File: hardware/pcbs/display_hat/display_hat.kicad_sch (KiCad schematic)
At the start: 13 parts, among them J1 WAVESHARE_HAT_HEADER, J2 MTA100_08, J3 MTA100_08, J4 MTA100_02

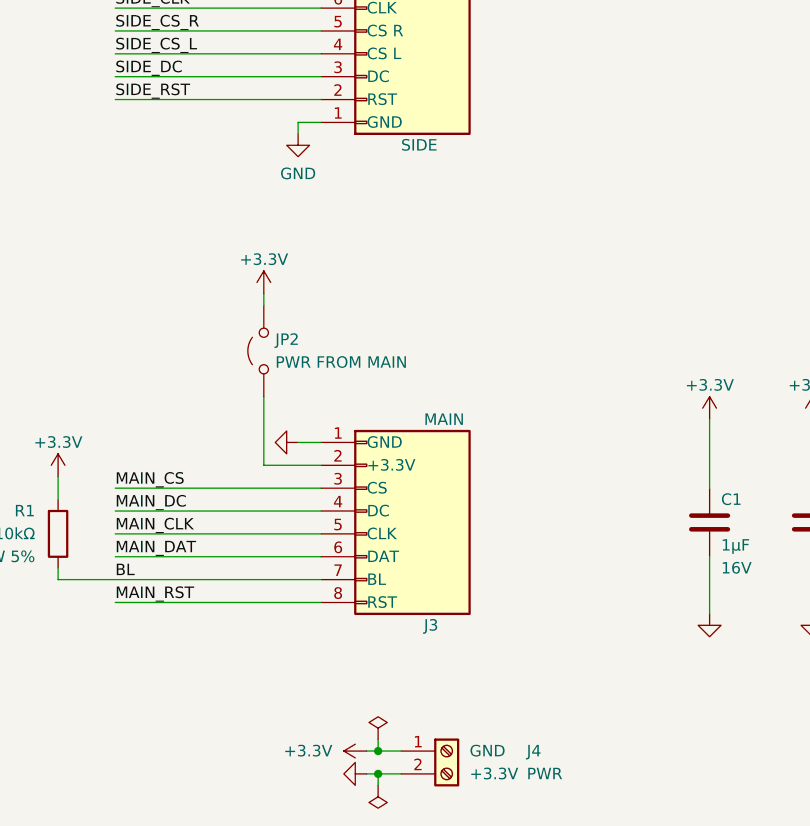
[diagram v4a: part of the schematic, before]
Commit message: display_hat: fix pin order for main connector
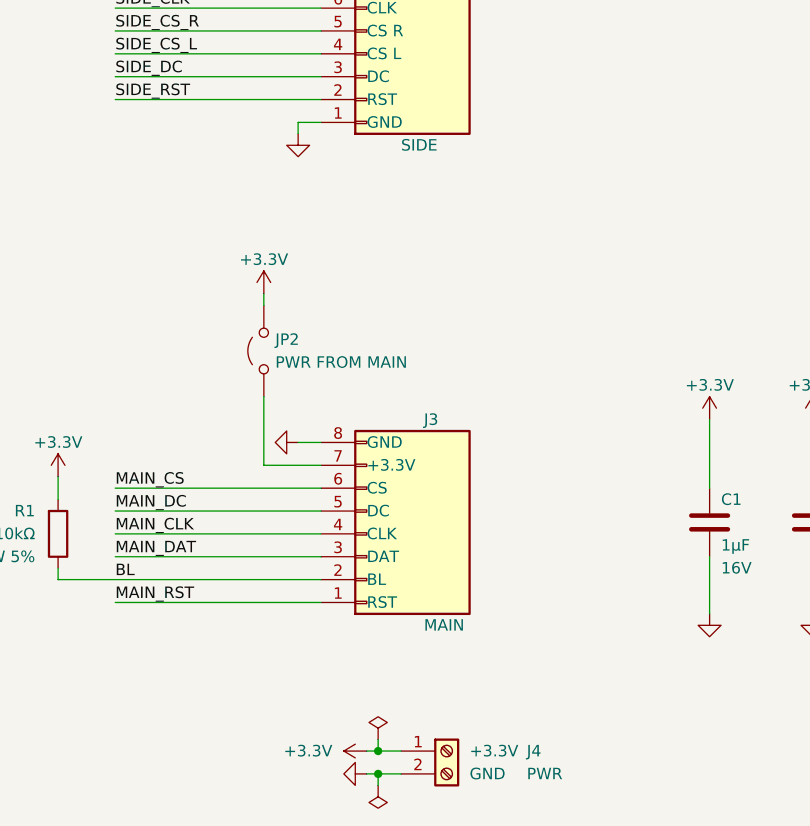
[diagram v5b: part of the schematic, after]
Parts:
- J3: Purpose Pin1 GND -> RST; Purpose Pin2 +3.3V -> BL; Purpose Pin3 CS -> DAT; Purpose Pin4 DC -> CLK; Purpose Pin5 CLK -> DC; Purpose Pin6 DAT -> CS; Purpose Pin7 BL -> +3.3V; Purpose Pin8 RST -> GND
- J4: Purpose Pin1 GND -> +3.3V; Purpose Pin2 +3.3V -> GND
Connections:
- net BL: now also J3.2 (Pin_2); no longer J3.7 (Pin_7)
- net GND: now also J3.8 (Pin_8); no longer J3.1 (Pin_1)
- net MAIN_CLK: now also J3.4 (Pin_4); no longer J3.5 (Pin_5)
- net MAIN_CS: now also J3.6 (Pin_6); no longer J3.3 (Pin_3)
- net MAIN_DAT: now also J3.3 (Pin_3); no longer J3.6 (Pin_6)
- net MAIN_DC: now also J3.5 (Pin_5); no longer J3.4 (Pin_4)
- net MAIN_RST: now also J3.1 (Pin_1); no longer J3.8 (Pin_8)
- net at JP2.1 (A): now also J3.7 (Pin_7); no longer J3.2 (Pin_2)
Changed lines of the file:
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@@
 			)
 		)
-		(property "Purpose Pin1" "GND"
+		(property "Purpose Pin1" "+3.3V"
 			(at 167.64 146.05 0)
 			(effects
@@
 			)
 		)
-		(property "Purpose Pin2" "+3.3V"
+		(property "Purpose Pin2" "GND"
 			(at 167.64 148.59 0)
 			(effects
@@
 	(symbol
 		(lib_id "conn:Conn_01x08")
-		(at 156.21 114.3 0)
+		(at 156.21 127 0)
+		(mirror x)
 		(unit 1)
 		(exclude_from_sim no)
@@
 		(dnp no)
 		(property "Reference" "J3"
+			(at 162.56 109.22 0)
+			(effects
+				(font
+					(size 1.27 1.27)
+				)
+				(justify left)
+			)
+		)
+		(property "Value" "MTA100_08"
+			(at 161.036 109.22 0)
+			(effects
+				(font
+					(size 1.27 1.27)
+				)
+				(hide yes)
+			)
+		)
+		(property "Footprint" "Connector_MTA-100:mta100_01x8_P2.54_640455-8"
+			(at 156.21 131.318 0)
+			(effects
+				(font
+					(size 1.27 1.27)
+				)
+				(hide yes)
+			)
+		)
+		(property "Datasheet" "~"
+			(at 156.21 127 0)
+			(effects
+				(font
+					(size 1.27 1.27)
+				)
+				(hide yes)
+			)
+		)
+		(property "Description" "Generic connector, single row, 01x06, script generated (kicad-library-utils/schlib/autogen/connector/)"
+			(at 156.464 131.318 0)
+			(effects
+				(font
+					(size 1.27 1.27)
+				)
+				(hide yes)
+			)
+		)
+		(property "Purpose Pin1" "RST"
+			(at 156.21 129.54 0)
+			(do_not_autoplace yes)
+			(effects
+				(font
+					(size 1.27 1.27)
+				)
+				(justify left)
+			)
+		)
+		(property "Purpose Pin2" "BL"
+			(at 156.21 127 0)
+			(do_not_autoplace yes)
+			(effects
+				(font
+					(size 1.27 1.27)
+				)
+				(justify left)
+			)
+		)
+		(property "Purpose Pin3" "DAT"
+			(at 156.21 124.46 0)
+			(do_not_autoplace yes)
+			(effects
+				(font
+					(size 1.27 1.27)
+				)
+				(justify left)
+			)
+		)
+		(property "Purpose Pin4" "CLK"
+			(at 156.21 121.92 0)
+			(do_not_autoplace yes)
+			(effects
+				(font
+					(size 1.27 1.27)
+				)
+				(justify left)
+			)
+		)
+		(property "Purpose Pin5" "DC"
+			(at 156.21 119.38 0)
+			(do_not_autoplace yes)
+			(effects
+				(font
+					(size 1.27 1.27)
+				)
+				(justify left)
+			)
+		)
+		(property "Purpose Pin6" "CS"
+			(at 156.21 116.84 0)
+			(do_not_autoplace yes)
+			(effects
+				(font
+					(size 1.27 1.27)
+				)
+				(justify left)
+			)
+		)
+		(property "Purpose Pin7" "+3.3V"
+			(at 156.21 114.3 0)
+			(do_not_autoplace yes)
+			(effects
+				(font
+					(size 1.27 1.27)
+				)
+				(justify left)
+			)
+		)
+		(property "Purpose Pin8" "GND"
+			(at 156.21 111.76 0)
+			(do_not_autoplace yes)
+			(effects
+				(font
+					(size 1.27 1.27)
+				)
+				(justify left)
+			)
+		)
+		(property "Purpose" "MAIN"
 			(at 162.56 132.08 0)
 			(effects
@@
 			)
 		)
-		(property "Value" "MTA100_08"
-			(at 161.036 132.08 0)
-			(effects
-				(font
-					(size 1.27 1.27)
-				)
-				(hide yes)
-			)
-		)
-		(property "Footprint" "Connector_MTA-100:mta100_01x8_P2.54_640455-8"
-			(at 156.21 109.982 0)
-			(effects
-				(font
-					(size 1.27 1.27)
-				)
-				(hide yes)
-			)
-		)
-		(property "Datasheet" "~"
-			(at 156.21 114.3 0)
-			(effects
-				(font
-					(size 1.27 1.27)
-				)
-				(hide yes)
-			)
-		)
-		(property "Description" "Generic connector, single row, 01x06, script generated (kicad-library-utils/schlib/autogen/connector/)"
-			(at 156.464 109.982 0)
-			(effects
-				(font
-					(size 1.27 1.27)
-				)
-				(hide yes)
-			)
-		)
-		(property "Purpose Pin1" "GND"
-			(at 156.21 111.76 0)
-			(do_not_autoplace yes)
-			(effects
-				(font
-					(size 1.27 1.27)
-				)
-				(justify left)
-			)
-		)
-		(property "Purpose Pin2" "+3.3V"
-			(at 156.21 114.3 0)
-			(do_not_autoplace yes)
-			(effects
-				(font
-					(size 1.27 1.27)
-				)
-				(justify left)
-			)
-		)
-		(property "Purpose Pin3" "CS"
-			(at 156.21 116.84 0)
-			(do_not_autoplace yes)
-			(effects
-				(font
-					(size 1.27 1.27)
-				)
-				(justify left)
-			)
-		)
-		(property "Purpose Pin4" "DC"
-			(at 156.21 119.38 0)
-			(do_not_autoplace yes)
-			(effects
-				(font
-					(size 1.27 1.27)
-				)
-				(justify left)
-			)
-		)
-		(property "Purpose Pin5" "CLK"
-			(at 156.21 121.92 0)
-			(do_not_autoplace yes)
-			(effects
-				(font
-					(size 1.27 1.27)
-				)
-				(justify left)
-			)
-		)
-		(property "Purpose Pin6" "DAT"
-			(at 156.21 124.46 0)
-			(do_not_autoplace yes)
-			(effects
-				(font
-					(size 1.27 1.27)
-				)
-				(justify left)
-			)
-		)
-		(property "Purpose Pin7" "BL"
+		(property "Part" "640456-8"
 			(at 156.21 127 0)
-			(do_not_autoplace yes)
-			(effects
-				(font
-					(size 1.27 1.27)
-				)
-				(justify left)
-			)
-		)
-		(property "Purpose Pin8" "RST"
-			(at 156.21 129.54 0)
-			(do_not_autoplace yes)
-			(effects
-				(font
-					(size 1.27 1.27)
-				)
-				(justify left)
-			)
-		)
-		(property "Purpose" "MAIN"
-			(at 162.56 109.22 0)
-			(effects
-				(font
-					(size 1.27 1.27)
-				)
-				(justify left)
-			)
-		)
-		(property "Part" "640456-8"
-			(at 156.21 114.3 0)
 			(effects
 				(font
@@
 		)
 		(property "Shop" "https://eu.mouser.com/ProductDetail/TE-Connectivity-AMP/640456-8?qs=%2F35zJ5USjomho1287DA4QA%3D%3D"
-			(at 156.21 114.3 0)
+			(at 156.21 127 0)
 			(effects
 				(font
@@
 					(size 1.27 1.27)
 				)
-			)
-		)
+				(hide yes)
+			)
+		)

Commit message: boards: update mta100 part numbers
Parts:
- J2, J3: Part 640456-8 -> 640457-8; Shop https://eu.mouser.com/ProductDetail/TE-Connectivity-AMP/640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 -> https://eu.mouser.com/ProductDetail/TE-Connectivity/640457-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
- J4: Part 640456-2 -> 640457-2; Shop https://eu.mouser.com/ProductDetail/TE-Connectivity-AMP/640456-2?qs=%2F35zJ5USjomRu3EJQJgZCQ%3D%3D -> https://eu.mouser.com/ProductDetail/TE-Connectivity-AMP/640457-2?qs=%2F35zJ5USjomWpIT3n5epmg%3D%3D
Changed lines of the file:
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@@
 			)
 		)
-		(property "Shop" "https://eu.mouser.com/ProductDetail/TE-Connectivity-AMP/640456-2?qs=%2F35zJ5USjomRu3EJQJgZCQ%3D%3D"
+		(property "Shop" "https://eu.mouser.com/ProductDetail/TE-Connectivity-AMP/640457-2?qs=%2F35zJ5USjomWpIT3n5epmg%3D%3D"
 			(at 165.1 146.05 0)
 			(effects
@@
 			)
 		)
-		(property "Part" "640456-2"
+		(property "Part" "640457-2"
 			(at 165.1 146.05 0)
 			(effects
@@
 			)
 		)
-		(property "Part" "640456-8"
+		(property "Part" "640457-8"
 			(at 156.21 127 0)
 			(effects
@@
 			)
 		)
-		(property "Shop" "https://eu.mouser.com/ProductDetail/TE-Connectivity-AMP/640456-8?qs=%2F35zJ5USjomho1287DA4QA%3D%3D"
+		(property "Shop" "https://eu.mouser.com/ProductDetail/TE-Connectivity/640457-8?qs=%2F35zJ5USjokX8LSglMnOhw%3D%3D"
 			(at 156.21 127 0)
 			(effects
@@
 			)
 		)
-		(property "Part" "640456-8"
+		(property "Part" "640457-8"
 			(at 156.21 73.66 0)
 			(effects
@@
 			)
 		)
-		(property "Shop" "https://eu.mouser.com/ProductDetail/TE-Connectivity-AMP/640456-8?qs=%2F35zJ5USjomho1287DA4QA%3D%3D"
+		(property "Shop" "https://eu.mouser.com/ProductDetail/TE-Connectivity/640457-8?qs=%2F35zJ5USjokX8LSglMnOhw%3D%3D"
 			(at 156.21 73.66 0)
 			(effects

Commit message: boards: update wrong shop links
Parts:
- C1, C2: Shop https://store.comet.bg/Catalogue/Product/16789/ -> https://store.comet.bg/Catalogue/Product/6645/
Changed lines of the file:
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@@
 			)
 		)
-		(property "Shop" "https://store.comet.bg/Catalogue/Product/16789/"
+		(property "Shop" "https://store.comet.bg/Catalogue/Product/6645/"
 			(at 205.74 120.65 0)
 			(effects
@@
 			)
 		)
-		(property "Shop" "https://store.comet.bg/Catalogue/Product/16789/"
+		(property "Shop" "https://store.comet.bg/Catalogue/Product/6645/"
 			(at 194.31 120.65 0)
 			(effects

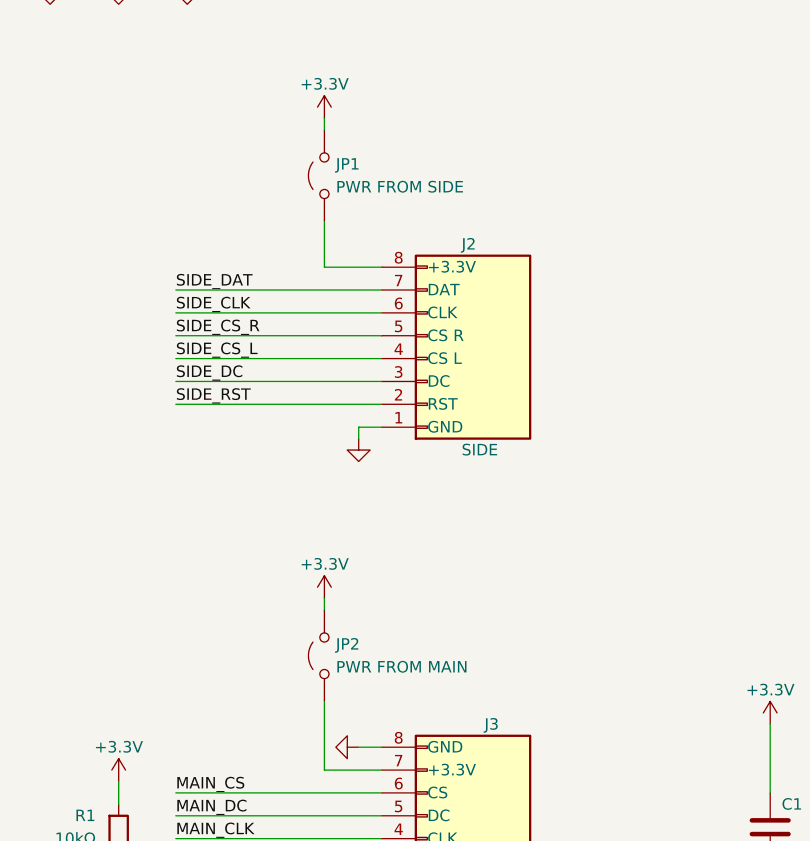
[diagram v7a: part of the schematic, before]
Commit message: hat_pcbs: more space under MTA100 connectors as per datasheet
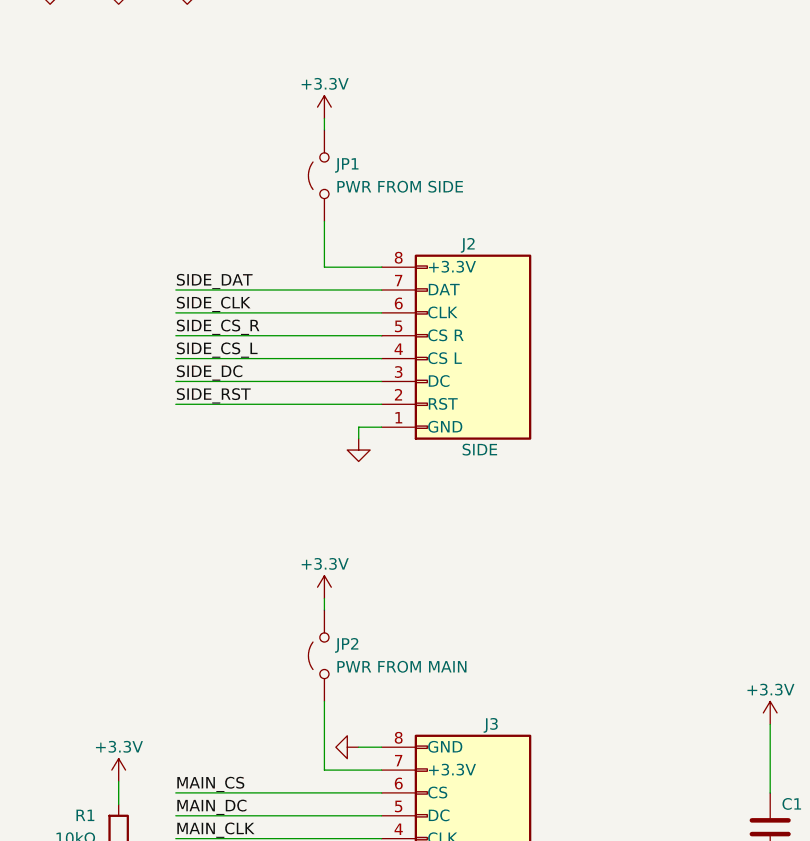
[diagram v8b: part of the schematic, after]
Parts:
- JP1, JP2: footprint Connector_PinHeader_2.54mm:PinHeader_1x02_P2.54mm_Vertical -> Connector_PinHeader_2.54mm:PinHeader_1x02_P2.54mm_Horizontal
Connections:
- net +3.3V: now also JP1.1 (A), JP2.1 (A); no longer JP1.2 (B), JP2.2 (B)
- net at J2.8 (Pin_8): now also JP1.2 (B); no longer JP1.1 (A)
- net at J3.7 (Pin_7): now also JP2.2 (B); no longer JP2.1 (A)
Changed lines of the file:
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@@
 		(lib_id "Jumper:Jumper_2_Open")
 		(at 144.78 48.26 90)
+		(mirror x)
 		(unit 1)
 		(exclude_from_sim yes)
@@
 		)
 		(property "Value" "PWR FROM SIDE"
-			(at 146.05 49.5299 90)
+			(at 146.05 49.53 90)
 			(effects
 				(font
@@
 			)
 		)
-		(property "Footprint" "Connector_PinHeader_2.54mm:PinHeader_1x02_P2.54mm_Vertical"
+		(property "Footprint" "Connector_PinHeader_2.54mm:PinHeader_1x02_P2.54mm_Horizontal"
 			(at 144.78 48.26 0)
 			(effects
@@
 		)
 		(property "Part" "Header_Angled_2"
-			(at 146.05 49.53 90)
+			(at 146.05 46.99 90)
 			(effects
 				(font
@@
 		(lib_id "Jumper:Jumper_2_Open")
 		(at 144.78 101.6 90)
+		(mirror x)
 		(unit 1)
 		(exclude_from_sim yes)
@@
 		)
 		(property "Value" "PWR FROM MAIN"
-			(at 146.05 102.8699 90)
+			(at 146.05 102.87 90)
 			(effects
 				(font
@@
 			)
 		)
-		(property "Footprint" "Connector_PinHeader_2.54mm:PinHeader_1x02_P2.54mm_Vertical"
+		(property "Footprint" "Connector_PinHeader_2.54mm:PinHeader_1x02_P2.54mm_Horizontal"
 			(at 144.78 101.6 0)
 			(effects
@@
 		)
 		(property "Part" "Header_Angled_2"
-			(at 146.05 102.87 90)
-			(effects
-				(font
+			(at 146.05 100.33 90)
+			(effects
+				(font
